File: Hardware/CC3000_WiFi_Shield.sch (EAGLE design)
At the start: 32 parts, among them J1 U.FL, U2 ARDUINO_SHIELDLABEL, U3 74HC4050, U4 USD-SOCKETNEW, U5 CC3000

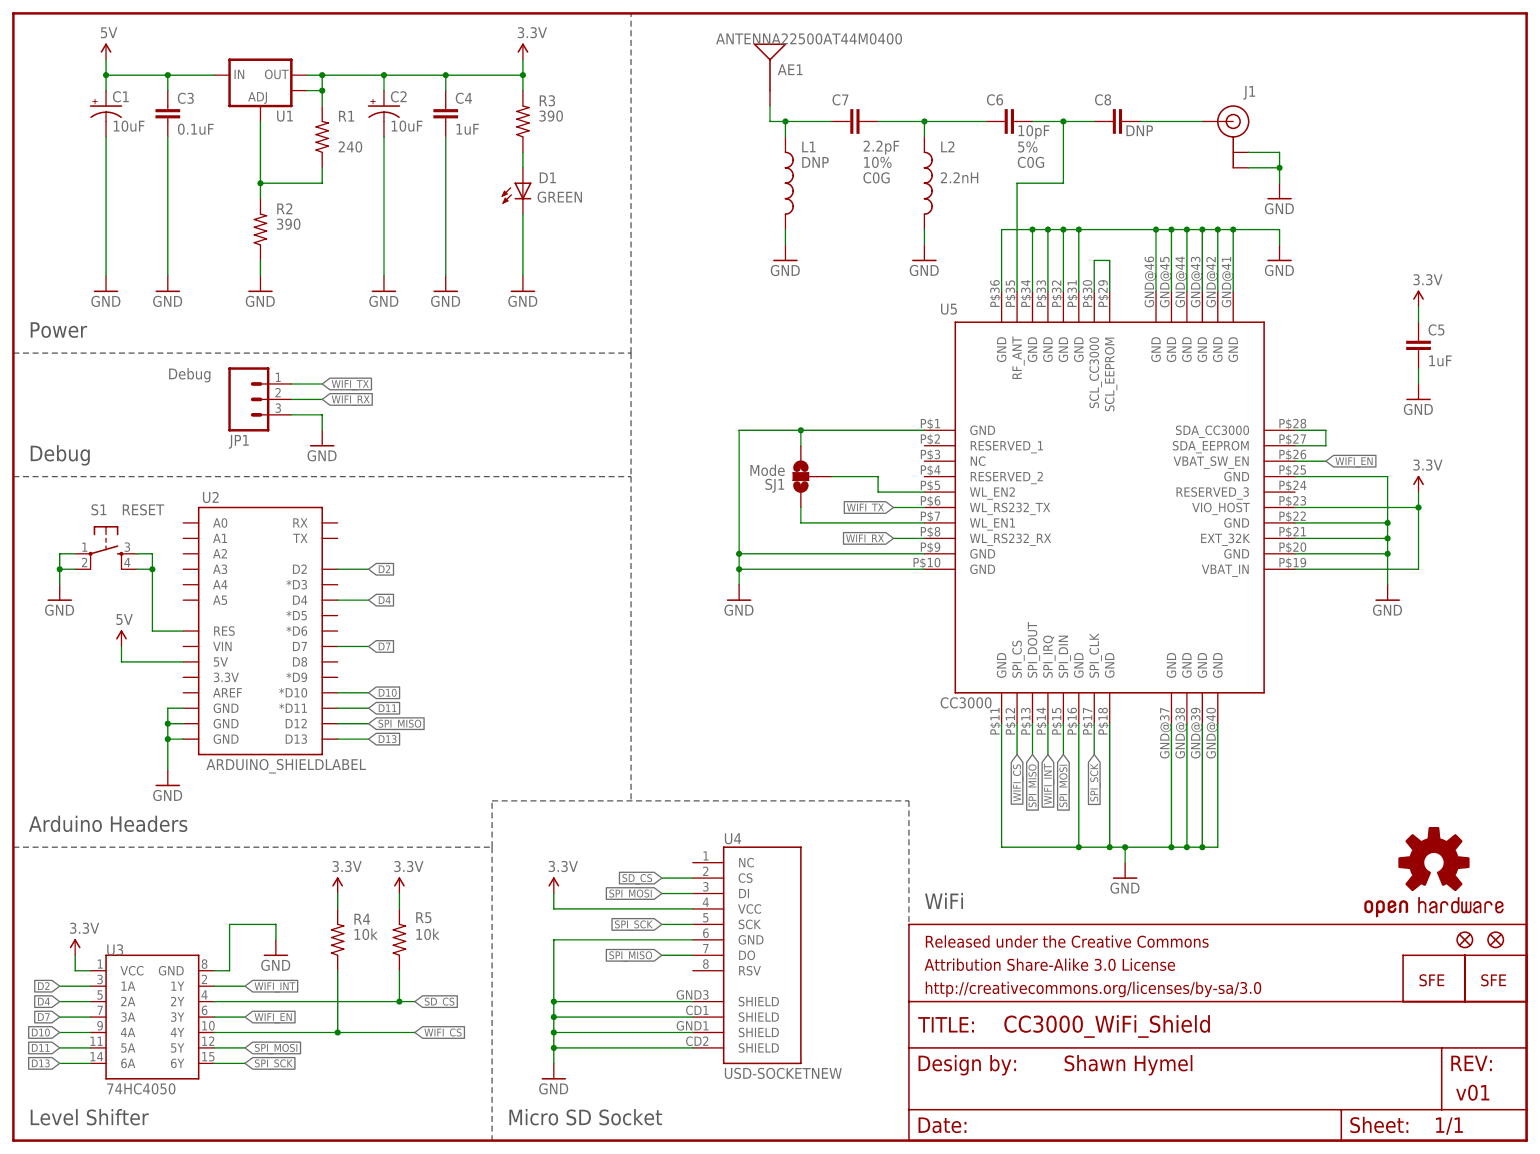
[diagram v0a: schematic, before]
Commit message: Added high-Z protection on MISO, replaced tantalums, added 2nd set of headers on shield
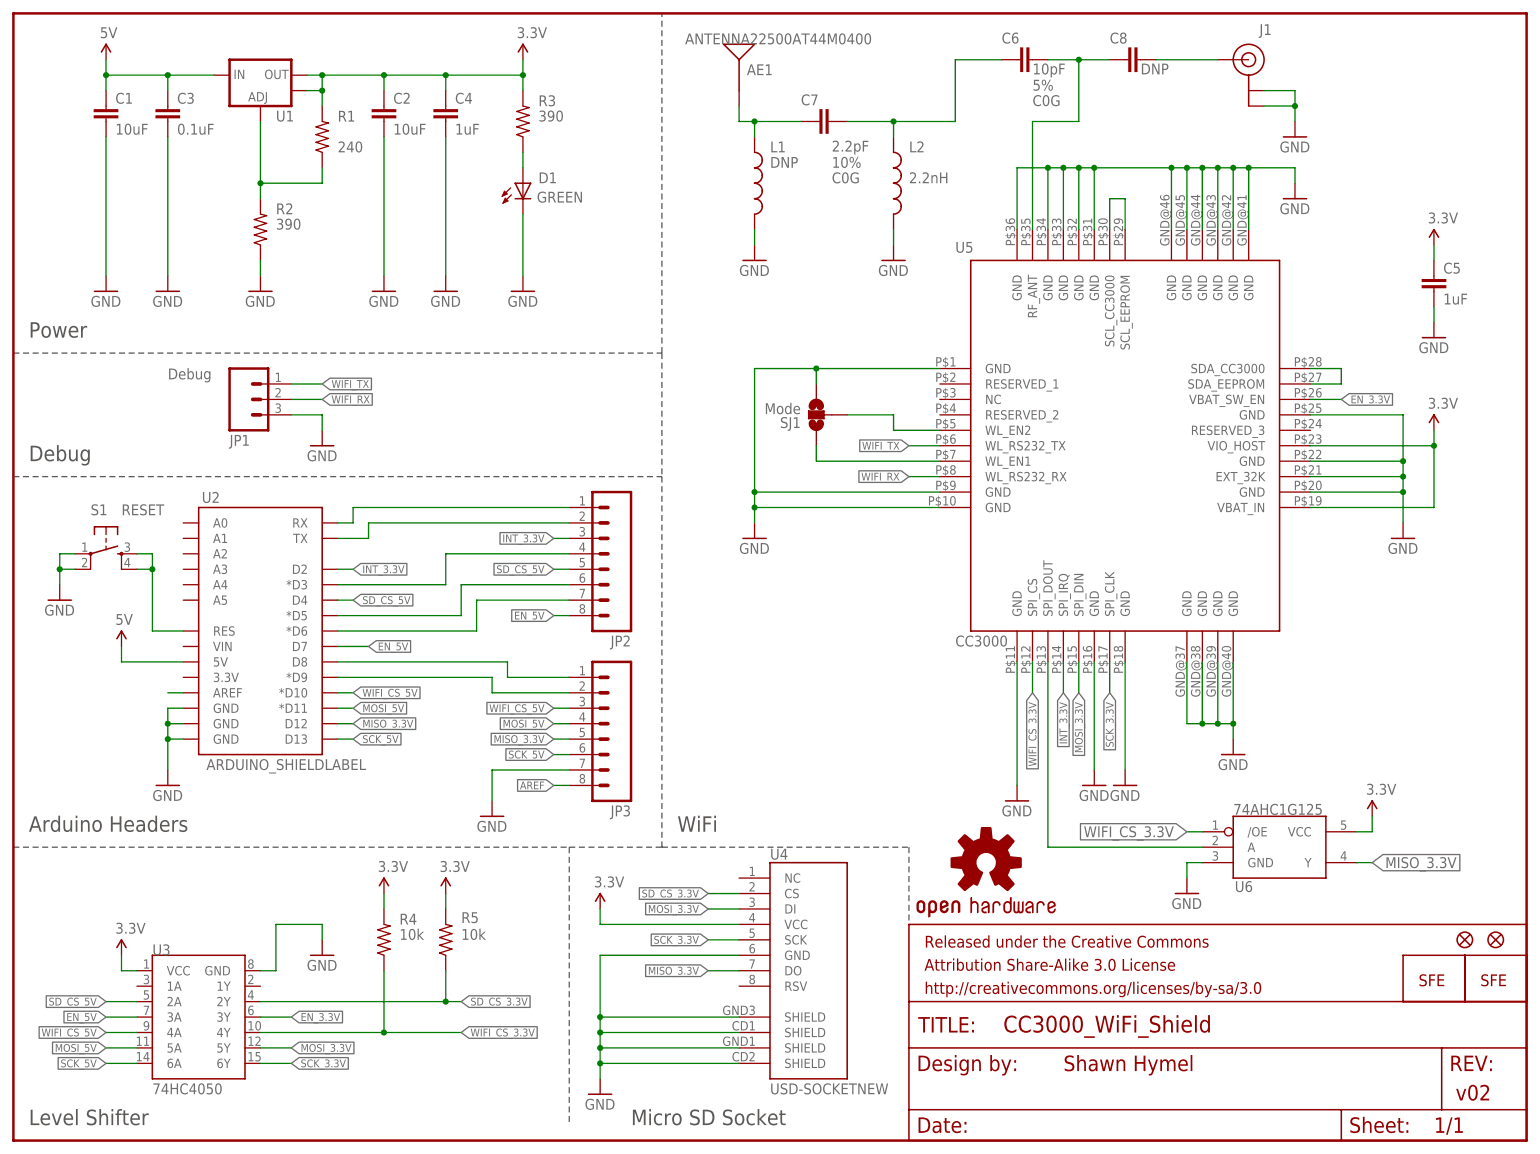
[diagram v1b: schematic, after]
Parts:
- added JP2, JP3: (no value), SparkFun-Connectors:M081X08
- added U6: 74AHC1G125, SparkFun-DigitalIC:74AHC1G125
- C1, C2: device SparkFun-Capacitors:CAP_POL1206 -> SparkFun-Capacitors:CAP0805
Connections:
- net SD_CS renamed SD_CS_3.3V
- net SPI_MOSI renamed MOSI_3.3V
- net SPI_SCK renamed SCK_3.3V
- net WIFI_EN renamed EN_3.3V
- removed net D10: U2.*D10, U3.4A
- removed net D11: U2.*D11, U3.5A
- removed net D13: U2.D13, U3.6A
- removed net D2: U2.D2, U3.1A
- removed net D4: U2.D4, U3.2A
- removed net D7: U2.D7, U3.3A
- removed net SPI_MISO: U2.D12, U4.DO, U5.SPI_DOUT
- removed net WIFI_CS: R4.1, U3.4Y, U5.SPI_CS
- removed net WIFI_INT: U3.1Y, U5.SPI_IRQ
- new net AREF: JP3.8, U2.AREF
- new net EN_5V: JP2.8, U2.D7, U3.3A
- new net INT_3.3V: JP2.3, U2.D2, U5.SPI_IRQ
- new net MISO_3.3V: JP3.5, U2.D12, U4.DO, U6.Y
- new net MOSI_5V: JP3.4, U2.*D11, U3.5A
- new net N$125: JP2.1, U2.RX
- new net N$126: JP2.2, U2.TX
- new net N$127: JP2.4, U2.*D3
- new net N$128: JP2.6, U2.*D5
- new net N$129: JP2.7, U2.*D6
- new net N$130: JP3.1, U2.D8
- new net N$131: JP3.2, U2.*D9
- new net SCK_5V: JP3.6, U2.D13, U3.6A
- new net SD_CS_5V: JP2.5, U2.D4, U3.2A
- new net WIFI_CS_3.3V: R4.1, U3.4Y, U5.SPI_CS, U6./OE
- new net WIFI_CS_5V: JP3.3, U2.*D10, U3.4A
- new net WIFI_MISO: U5.SPI_DOUT, U6.A
- net 3.3V: now also C2.1, U6.VCC; no longer C2.+
- net 5V: now also C1.1; no longer C1.+
- net GND: now also C1.2, C2.2, JP3.7, U6.GND; no longer C1.-, C2.-
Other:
- note added: "v02"
- note removed: "v01"
- moved on the sheet: AE1, C5, C6, C7, C8, J1, L1, L2, R4, R5, SJ1, U3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

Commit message: Made corrections to schematic/board from first prototype
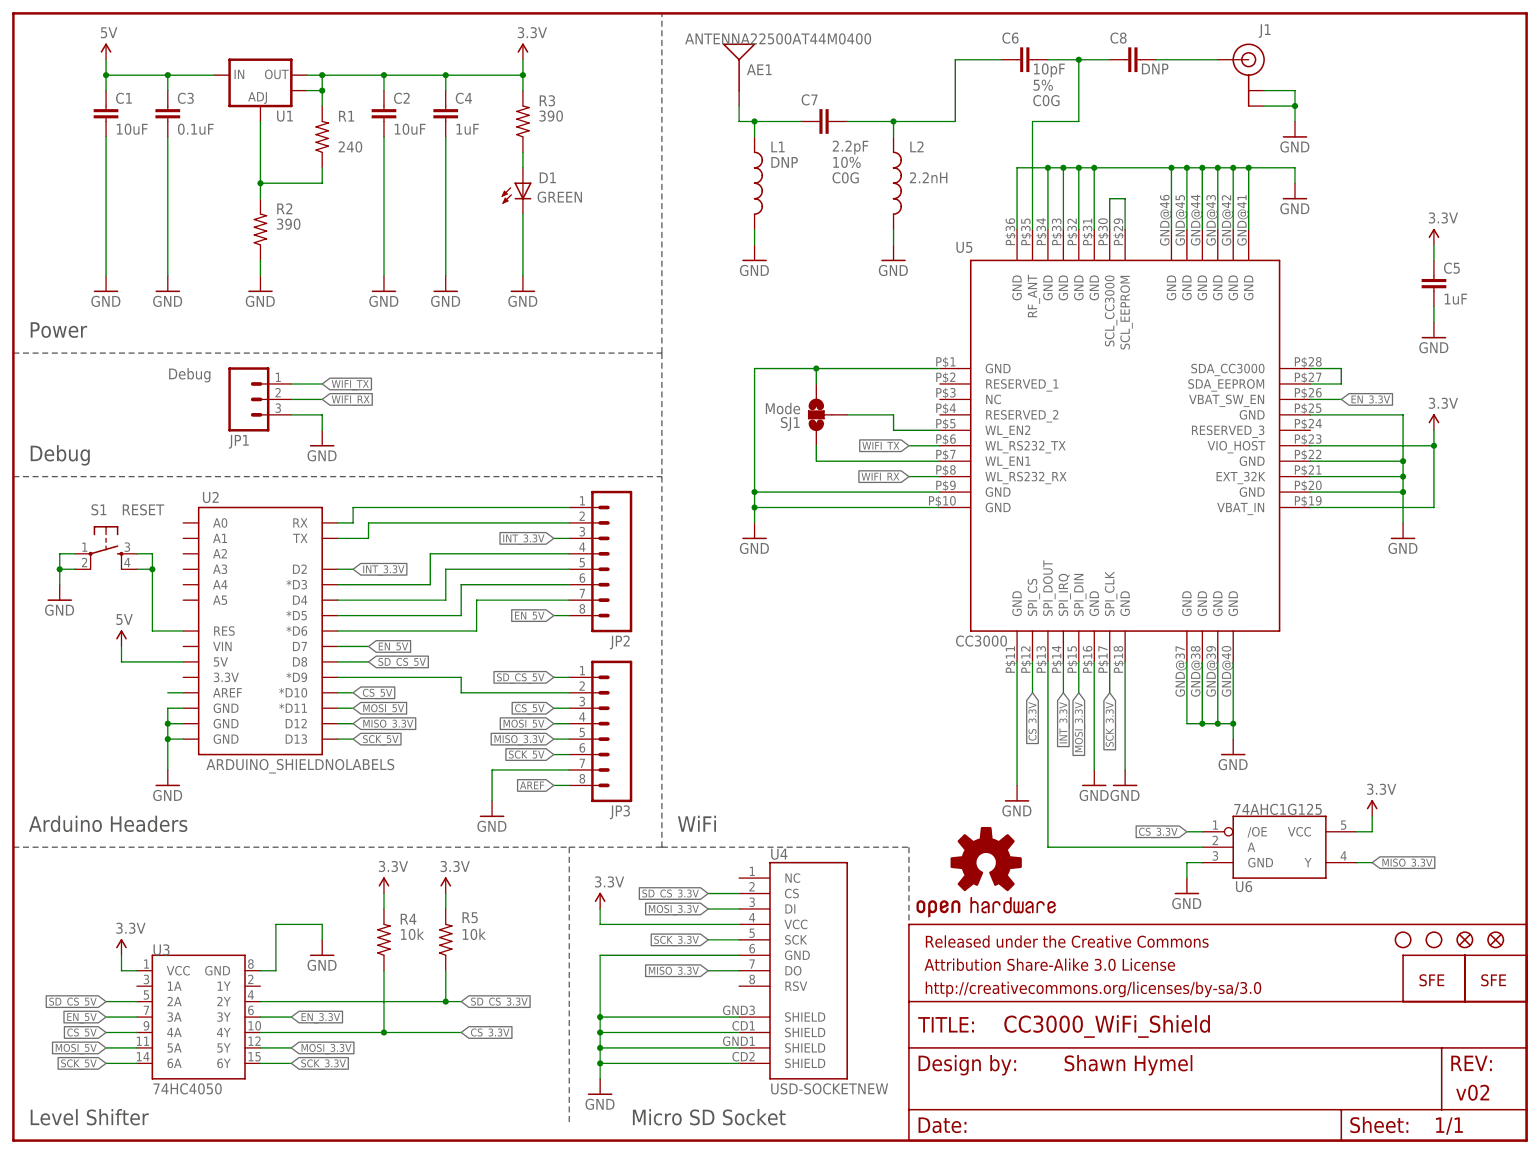
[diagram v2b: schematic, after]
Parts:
- added STANDOFF1, STANDOFF2: STAND-OFF, SparkFun-Electromechanical:STAND-OFF
- U2: value ARDUINO_SHIELDLABEL -> ARDUINO_SHIELDNOLABELS; device SparkFun-Boards:ARDUINO_SHIELDLABEL -> SparkFun-Boards:ARDUINO_SHIELDNOLABELS
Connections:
- net WIFI_CS_3.3V renamed CS_3.3V
- net WIFI_CS_5V renamed CS_5V
- net N$130: now also JP2.5, U2.D4; no longer JP3.1, U2.D8
- net SD_CS_5V: now also JP3.1, U2.D8; no longer JP2.5, U2.D4
